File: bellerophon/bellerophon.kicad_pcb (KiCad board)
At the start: 2 copper layers, 55 x 98 mm, 34 parts, among them Q1 ST3413A, Q2 IRLL014NPBF, Q3 IRLL014NPBF, U1 HT7350-A, U2 Adafruit_ICM20948, U3 MPL3115A2, U4 Teensy4.0, U5 XTSD

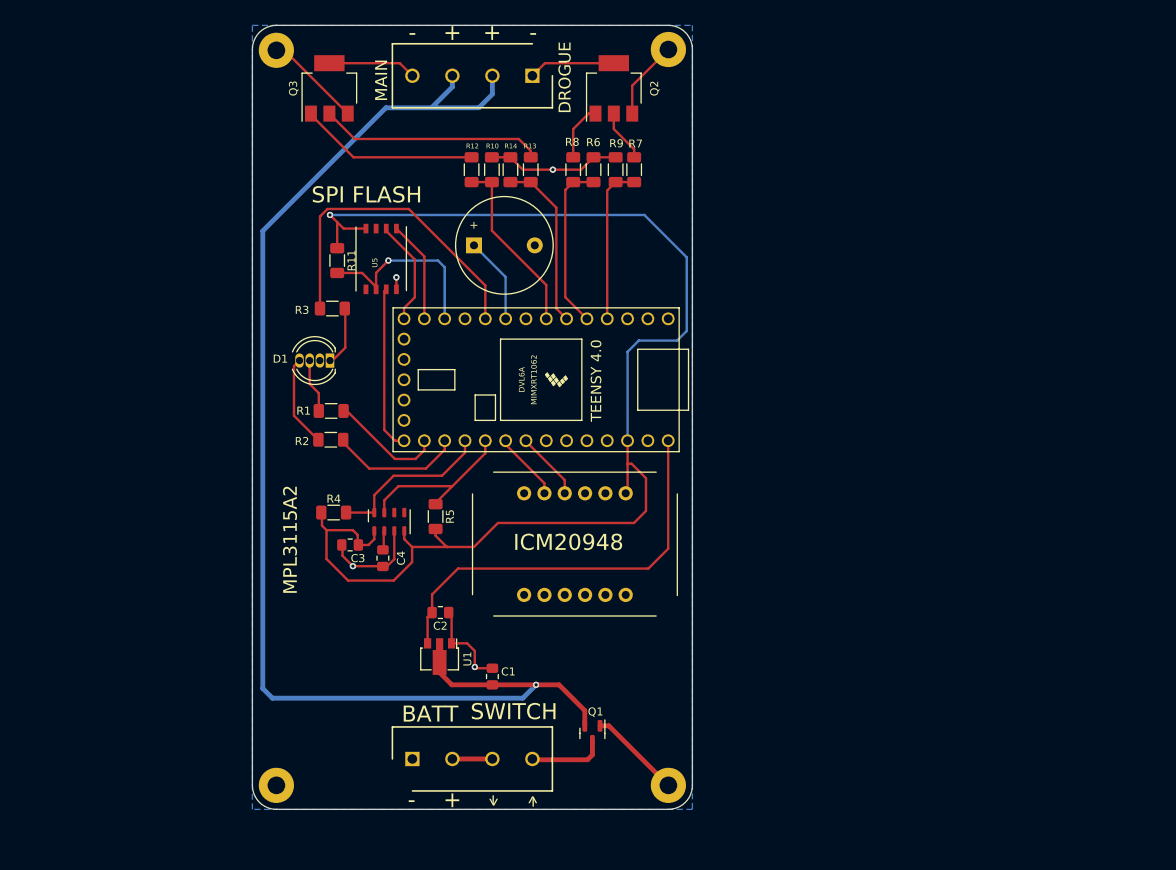
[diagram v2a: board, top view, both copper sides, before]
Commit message: add bno055 circuit to pcb, design new draft layout for SMT
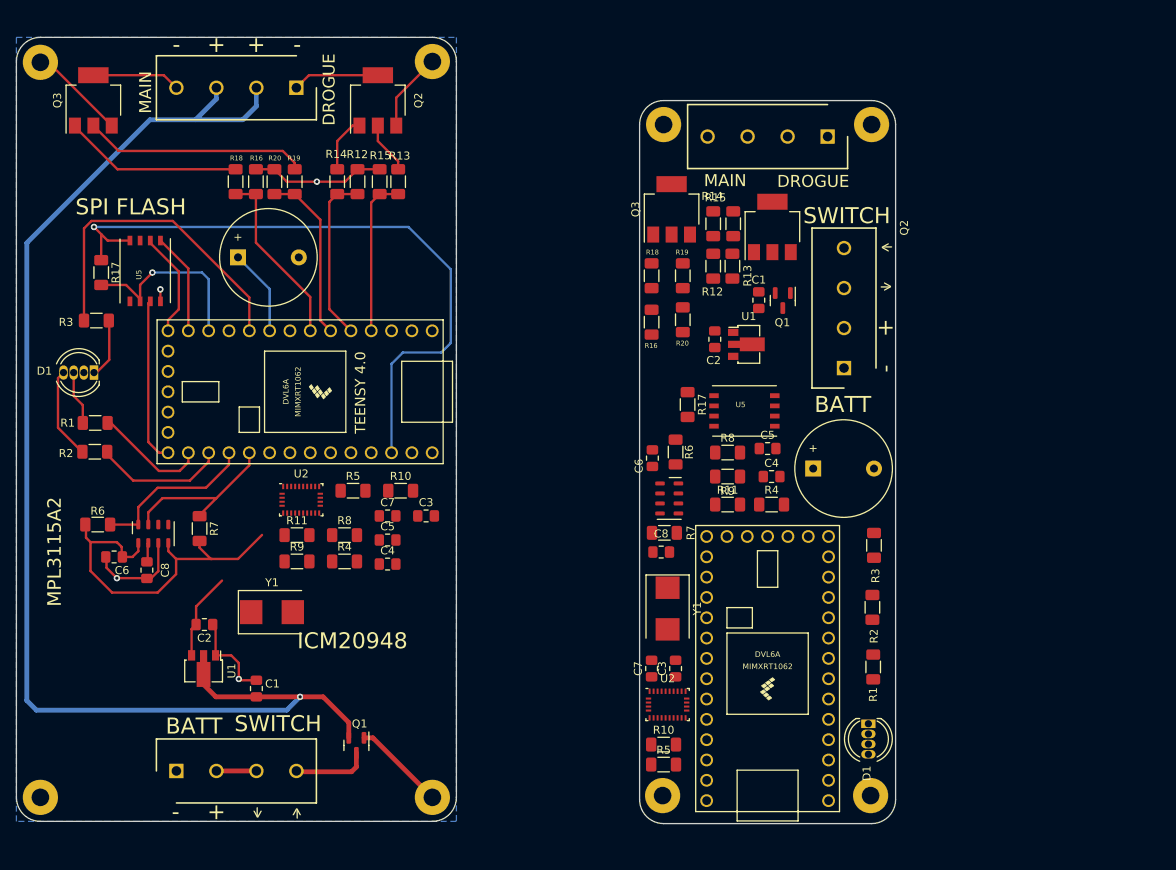
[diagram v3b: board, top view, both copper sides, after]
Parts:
- removed the H3 at (128.0, 51.1)
- removed the H4 at (177.0, 51.0)
- removed the U2 at (167.1, 126.1)
- added BZ1: Buzzer, Buzzer:PiezoBuzzer-PS1240, F.Cu at (123.2, 77.0)
- added C1: 1 µF, Capacitor_SMD:C_0805_2012Metric_Pad1.18x1.45mm_HandSolder, F.Cu at (125.5, 130.9)
- added C2: 1 µF, Capacitor_SMD:C_0805_2012Metric_Pad1.18x1.45mm_HandSolder, F.Cu at (119.0, 122.9)
- added C3: 22pF, Capacitor_SMD:C_0805_2012Metric_Pad1.18x1.45mm_HandSolder, F.Cu at (146.7, 109.3)
- added C3: 22pF, Capacitor_SMD:C_0805_2012Metric_Pad1.18x1.45mm_HandSolder, F.Cu at (177.9, 128.4)
- added C4: 22pF, Capacitor_SMD:C_0805_2012Metric_Pad1.18x1.45mm_HandSolder, F.Cu at (141.9, 115.3)
- added C4: 22pF, Capacitor_SMD:C_0805_2012Metric_Pad1.18x1.45mm_HandSolder, F.Cu at (189.9, 104.4)
- added C5: 0.1uF, Capacitor_SMD:C_0805_2012Metric_Pad1.18x1.45mm_HandSolder, F.Cu at (189.4, 100.9)
- added C5: 0.1uF, Capacitor_SMD:C_0805_2012Metric_Pad1.18x1.45mm_HandSolder, F.Cu at (141.9, 112.3)
- added C6: 0.1µF, Capacitor_SMD:C_0805_2012Metric_Pad1.18x1.45mm_HandSolder, F.Cu at (107.7, 114.5)
- added C7: 0.1uF, Capacitor_SMD:C_0805_2012Metric_Pad1.18x1.45mm_HandSolder, F.Cu at (141.9, 109.3)
- added C7: 0.1uF, Capacitor_SMD:C_0805_2012Metric_Pad1.18x1.45mm_HandSolder, F.Cu at (174.9, 128.4)
- added C8: 0.1µF, Capacitor_SMD:C_0805_2012Metric_Pad1.18x1.45mm_HandSolder, F.Cu at (111.8, 116.1)
- added D1: RGB LED, LED_THT:LED_D5.0mm-4_RGB, F.Cu at (105.2, 91.4)
- added H3: MountingHole_Pad, MountingHole:MountingHole_2.2mm_M2_Pad, F.Cu at (98.5, 52.6)
- added H3: MountingHole_Pad, MountingHole:MountingHole_2.2mm_M2_Pad, F.Cu at (176.4, 60.4)
- added H3: MountingHole_Pad, MountingHole:MountingHole_2.2mm_M2_Pad, F.Cu at (202.3, 144.3)
- added H4: MountingHole_Pad, MountingHole:MountingHole_2.2mm_M2_Pad, F.Cu at (147.5, 52.5)
- added H4: MountingHole_Pad, MountingHole:MountingHole_2.2mm_M2_Pad, F.Cu at (176.3, 144.3)
- added H4: MountingHole_Pad, MountingHole:MountingHole_2.2mm_M2_Pad, F.Cu at (202.4, 60.4)
- added PYRO1: Screw_Terminal_01x04, RS-Components:SHDR4W100P0X500_1X4_2000X800X1000P, F.Cu at (130.5, 55.8)
- added Q1: ST3413A, Package_TO_SOT_SMD:SOT-23, F.Cu at (138.0, 138.0)
- added Q2: IRLL014NPBF, Package_TO_SOT_SMD:SOT-223-3_TabPin2, F.Cu at (140.7, 57.4)
- added Q3: IRLL014NPBF, Package_TO_SOT_SMD:SOT-223-3_TabPin2, F.Cu at (105.1, 57.4)
- added R1: 225 ohm, Resistor_SMD:R_1206_3216Metric_Pad1.30x1.75mm_HandSolder, F.Cu at (105.3, 97.7)
- added R10: 10k ohms, Resistor_SMD:R_1206_3216Metric_Pad1.30x1.75mm_HandSolder, F.Cu at (143.5, 106.2)
- added R10: 10k ohms, Resistor_SMD:R_1206_3216Metric_Pad1.30x1.75mm_HandSolder, F.Cu at (176.4, 137.9)
- added R11: 10k ohms, Resistor_SMD:R_1206_3216Metric_Pad1.30x1.75mm_HandSolder, F.Cu at (184.4, 107.9)
- added R11: 10k ohms, Resistor_SMD:R_1206_3216Metric_Pad1.30x1.75mm_HandSolder, F.Cu at (130.6, 111.7)
- added R12: 470 ohms, Resistor_SMD:R_1206_3216Metric_Pad1.30x1.75mm_HandSolder, F.Cu at (138.1, 67.5)
- added R13: 49.9k ohms, Resistor_SMD:R_1206_3216Metric_Pad1.30x1.75mm_HandSolder, F.Cu at (140.9, 67.5)
- added R14: 470 ohms, Resistor_SMD:R_1206_3216Metric_Pad1.30x1.75mm_HandSolder, F.Cu at (135.6, 67.5)
- added R15: 100k ohms, Resistor_SMD:R_1206_3216Metric_Pad1.30x1.75mm_HandSolder, F.Cu at (143.2, 67.5)
- added R16: 470 ohms, Resistor_SMD:R_1206_3216Metric_Pad1.30x1.75mm_HandSolder, F.Cu at (125.4, 67.5)
- added R17: 10k ohms, Resistor_SMD:R_1206_3216Metric_Pad1.30x1.75mm_HandSolder, F.Cu at (106.1, 78.9)
- added R18: 470 ohms, Resistor_SMD:R_1206_3216Metric_Pad1.30x1.75mm_HandSolder, F.Cu at (122.9, 67.5)
- added R19: 100k ohms, Resistor_SMD:R_1206_3216Metric_Pad1.30x1.75mm_HandSolder, F.Cu at (130.3, 67.5)
- added R2: 225 ohm, Resistor_SMD:R_1206_3216Metric_Pad1.30x1.75mm_HandSolder, F.Cu at (105.3, 101.3)
- added R20: 49.9k ohms, Resistor_SMD:R_1206_3216Metric_Pad1.30x1.75mm_HandSolder, F.Cu at (127.8, 67.5)
- added R3: 225 ohm, Resistor_SMD:R_1206_3216Metric_Pad1.30x1.75mm_HandSolder, F.Cu at (105.5, 84.9)
- added R4: 10k ohms, Resistor_SMD:R_1206_3216Metric_Pad1.30x1.75mm_HandSolder, F.Cu at (189.9, 107.9)
- added R4: 10k ohms, Resistor_SMD:R_1206_3216Metric_Pad1.30x1.75mm_HandSolder, F.Cu at (136.5, 115.0)
- added R5: 10k ohms, Resistor_SMD:R_1206_3216Metric_Pad1.30x1.75mm_HandSolder, F.Cu at (137.6, 106.2)
- added R5: 10k ohms, Resistor_SMD:R_1206_3216Metric_Pad1.30x1.75mm_HandSolder, F.Cu at (176.4, 140.4)
- added R6: 4.7k ohms, Resistor_SMD:R_1206_3216Metric_Pad1.30x1.75mm_HandSolder, F.Cu at (105.7, 110.4)
- added R7: 4.7k ohms, Resistor_SMD:R_1206_3216Metric_Pad1.30x1.75mm_HandSolder, F.Cu at (118.4, 110.9)
- added R8: 10k ohms, Resistor_SMD:R_1206_3216Metric_Pad1.30x1.75mm_HandSolder, F.Cu at (184.4, 101.4)
- added R8: 10k ohms, Resistor_SMD:R_1206_3216Metric_Pad1.30x1.75mm_HandSolder, F.Cu at (136.5, 111.7)
- added R9: 10k ohms, Resistor_SMD:R_1206_3216Metric_Pad1.30x1.75mm_HandSolder, F.Cu at (184.4, 104.4)
- added R9: 10k ohms, Resistor_SMD:R_1206_3216Metric_Pad1.30x1.75mm_HandSolder, F.Cu at (130.6, 115.0)
- added TERMINAL1: Screw_Terminal_01x04, RS-Components:SHDR4W100P0X500_1X4_2000X800X1000P, F.Cu at (115.5, 141.2)
- added U1: HT7350-A, Package_TO_SOT_SMD:SOT-89-3, F.Cu at (118.9, 128.4)
- added U2: BNO055, Package_LGA:LGA-28_5.2x3.8mm_P0.5mm, F.Cu at (176.9, 132.9)
- added U2: BNO055, Package_LGA:LGA-28_5.2x3.8mm_P0.5mm, F.Cu at (131.1, 107.3)
- added U3: MPL3115A2, Package_LGA:NXP_LGA-8_3x5mm_P1.25mm_H1.1mm, F.Cu at (112.6, 111.5)
- added U4: Teensy4.0, teensy:Teensy40, F.Cu at (131.0, 93.8)
- added U5: XTSD, XTSD:LGA8_8X6, F.Cu at (111.6, 78.7)
- added Y1: 32.768kHz, Crystal:Crystal_SMD_7050-2Pin_7.0x5.0mm, F.Cu at (127.5, 121.3)
- added Y1: 32.768kHz, Crystal:Crystal_SMD_7050-2Pin_7.0x5.0mm, F.Cu at (176.9, 120.9)
- moved D1 81.2 mm to (202.0, 135.3), turned to -90 degrees
- moved R1 74.9 mm to (202.6, 128.2), turned to 90 degrees
- moved R3 73.9 mm to (202.7, 113.0), turned to -90 degrees
- moved TERMINAL1 72.8 mm to (198.9, 90.8), turned to 90 degrees
- moved R2 70.9 mm to (202.5, 120.8), turned to 90 degrees
- moved Q1 59.1 mm to (191.3, 82.4)
- moved C1 57.6 mm to (188.3, 82.3), turned to 90 degrees
- moved U1 54.7 mm to (186.8, 87.9), turned to 0 degrees
- moved BZ1 50.8 mm to (195.1, 103.4)
- moved U5 49.2 mm to (186.5, 96.2), turned to 0 degrees
- moved C2 48.4 mm to (182.8, 87.2), turned to -90 degrees
- moved R17 47.4 mm to (179.4, 95.4)
- moved U4 46.3 mm to (189.4, 128.4), turned to 90 degrees
- moved Q3 45.4 mm to (177.4, 71.0)
- moved R6 43.4 mm to (177.9, 101.3), turned to 90 degrees
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- renumbered C3 to C6, C4 to C8, R6 to R12, R7 to R13, R8 to R14, R9 to R15, R10 to R16, R11 to R17, R12 to R18, R13 to R19, R14 to R20, R4 to R6, R5 to R7
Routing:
- net +5V: track 51.7 -> 10.9 mm
- net +3.3V: track 163.9 -> 131.0 mm
- net /SCL0: track 8.58 -> 0.08 mm
- net /SDA0: track 8.58 -> 0.47 mm
- net GND: track 75.8 -> 77.4 mm
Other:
- board size 55 x 98 mm -> 109.9 x 98.3 mm
- copper layers 2 -> 4

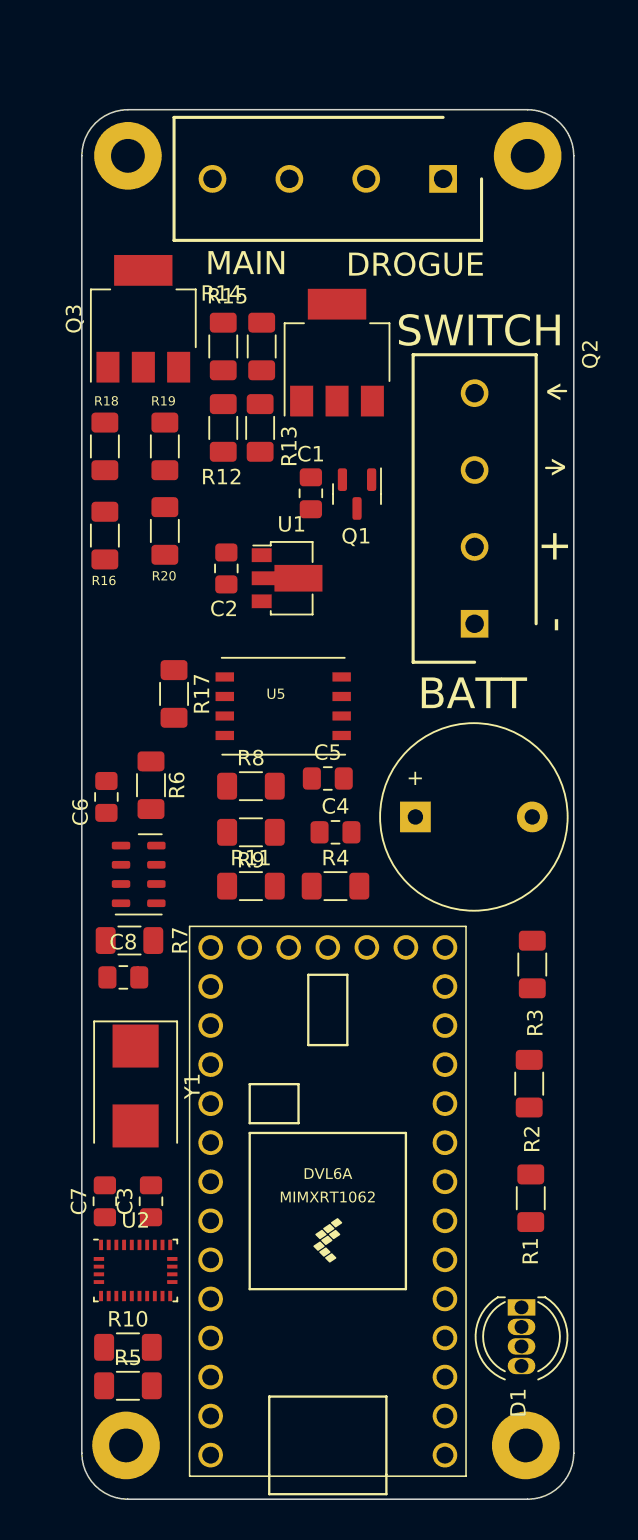
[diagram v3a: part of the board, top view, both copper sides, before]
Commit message: change sensor resistor to 0805
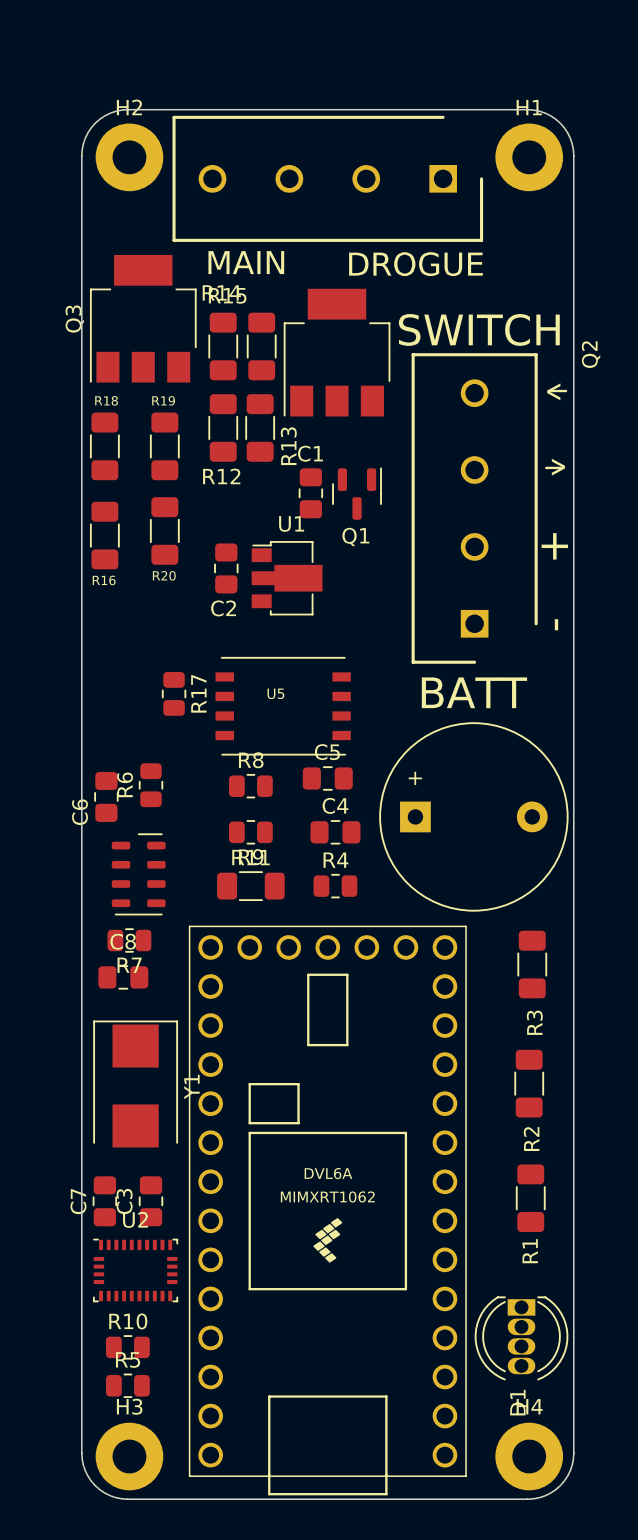
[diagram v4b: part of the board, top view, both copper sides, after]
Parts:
- removed the H3 at (176.4, 60.4)
- removed the H3 at (202.3, 144.3)
- removed the H4 at (176.3, 144.3)
- removed the H4 at (202.4, 60.4)
- added H1: MountingHole_Pad, MountingHole:MountingHole_2.2mm_M2_Pad, F.Cu at (202.5, 60.5)
- added H2: MountingHole_Pad, MountingHole:MountingHole_2.2mm_M2_Pad, F.Cu at (176.5, 60.5)
- added H3: MountingHole_Pad, MountingHole:MountingHole_2.2mm_M2_Pad, F.Cu at (176.5, 145.0)
- added H4: MountingHole_Pad, MountingHole:MountingHole_2.2mm_M2_Pad, F.Cu at (202.5, 145.0)
- R10, R17, R4, R5, R6, R7, R8, R9: footprint Resistor_SMD:R_1206_3216Metric_Pad1.30x1.75mm_HandSolder -> Resistor_SMD:R_0805_2012Metric
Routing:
- net GND: track 77.4 -> 76.4 mm

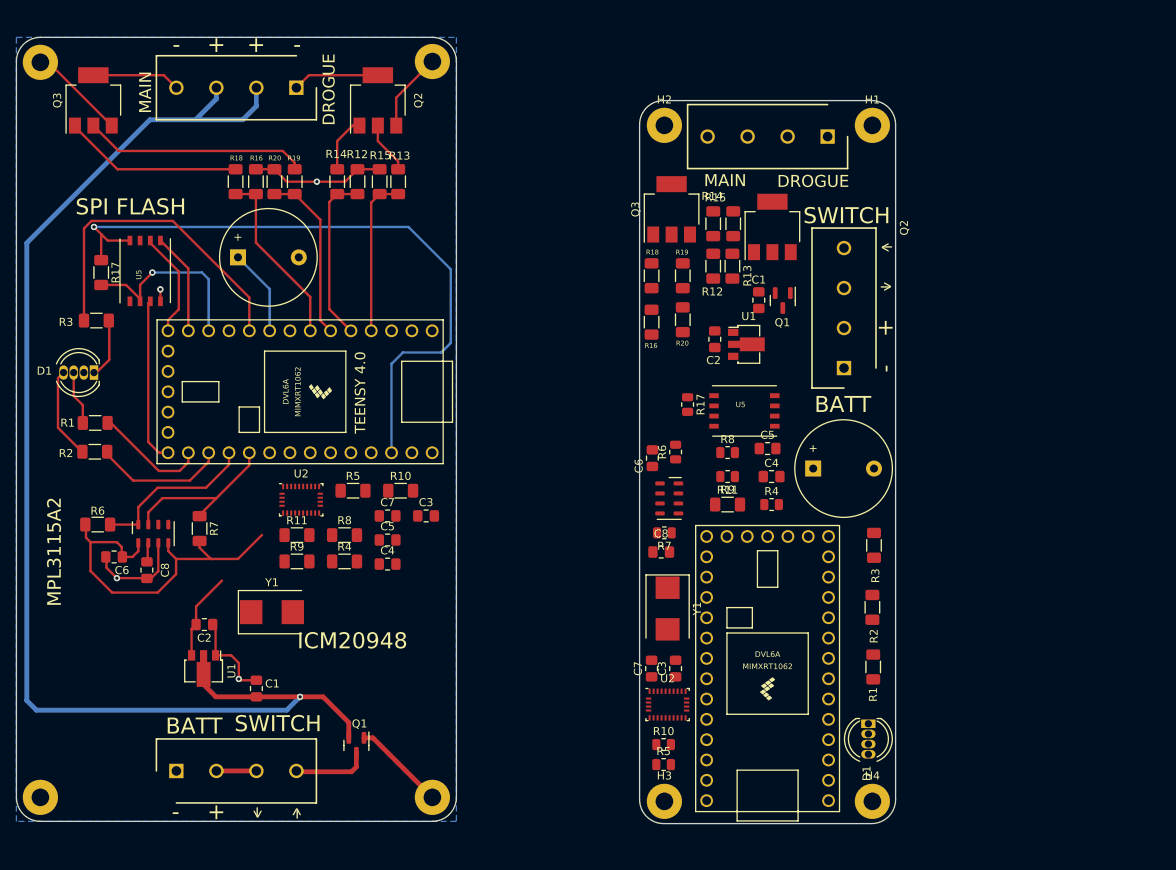
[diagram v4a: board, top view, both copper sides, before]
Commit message: change mount holes to m3, resize board
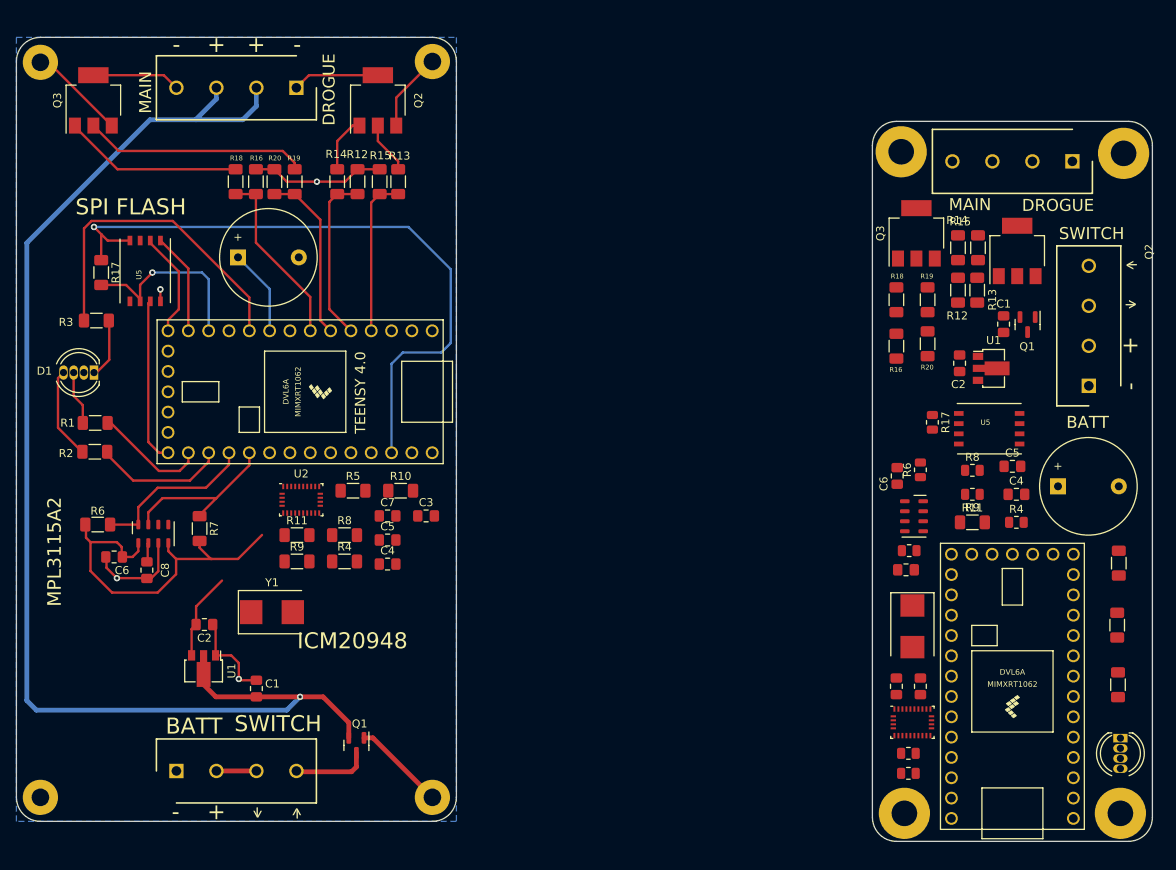
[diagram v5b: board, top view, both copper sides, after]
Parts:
- H1, H2, H3, H4: footprint MountingHole:MountingHole_2.2mm_M2_Pad -> MountingHole:MountingHole_3.2mm_M3_Pad
- R1, R2, R3: value 225 ohm -> 225
- R10, R11, R17, R4, R5, R8, R9: value 10k ohms -> 10k
- R12, R14, R16, R18: value 470 ohms -> 470
- R13, R20: value 49.9k ohms -> 49.9k
- R15, R19: value 100k ohms -> 100k
- R6, R7: value 4.7k ohms -> 4.7k
- moved H1 31.6 mm to (233.9, 64.0)
- moved D1 31.6 mm to (233.5, 137.1)
- moved H4 31.0 mm to (233.5, 146.5)
- moved PYRO1 30.8 mm to (227.5, 65.0)
- moved C1 30.7 mm to (218.9, 85.3)
- moved C2 30.7 mm to (213.4, 90.2)
- moved Q1 30.7 mm to (221.9, 85.4)
- moved Q2 30.7 mm to (220.6, 76.2)
- moved Q3 30.7 mm to (208.0, 74.0)
- moved R12 30.7 mm to (213.2, 81.1)
- moved R13 30.7 mm to (215.6, 81.1)
- moved R14 30.7 mm to (213.2, 75.8)
- moved R15 30.7 mm to (215.7, 75.8)
- moved R16 30.7 mm to (205.5, 88.1)
- moved R18 30.7 mm to (205.5, 82.3)
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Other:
- board size 109.9 x 98.3 mm -> 142 x 100.5 mm
